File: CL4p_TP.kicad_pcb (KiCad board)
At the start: 2 copper layers, 75.4 x 74.9 mm, 23 parts, among them U1 MCP23017, X1 Badgelife_shitty_connector

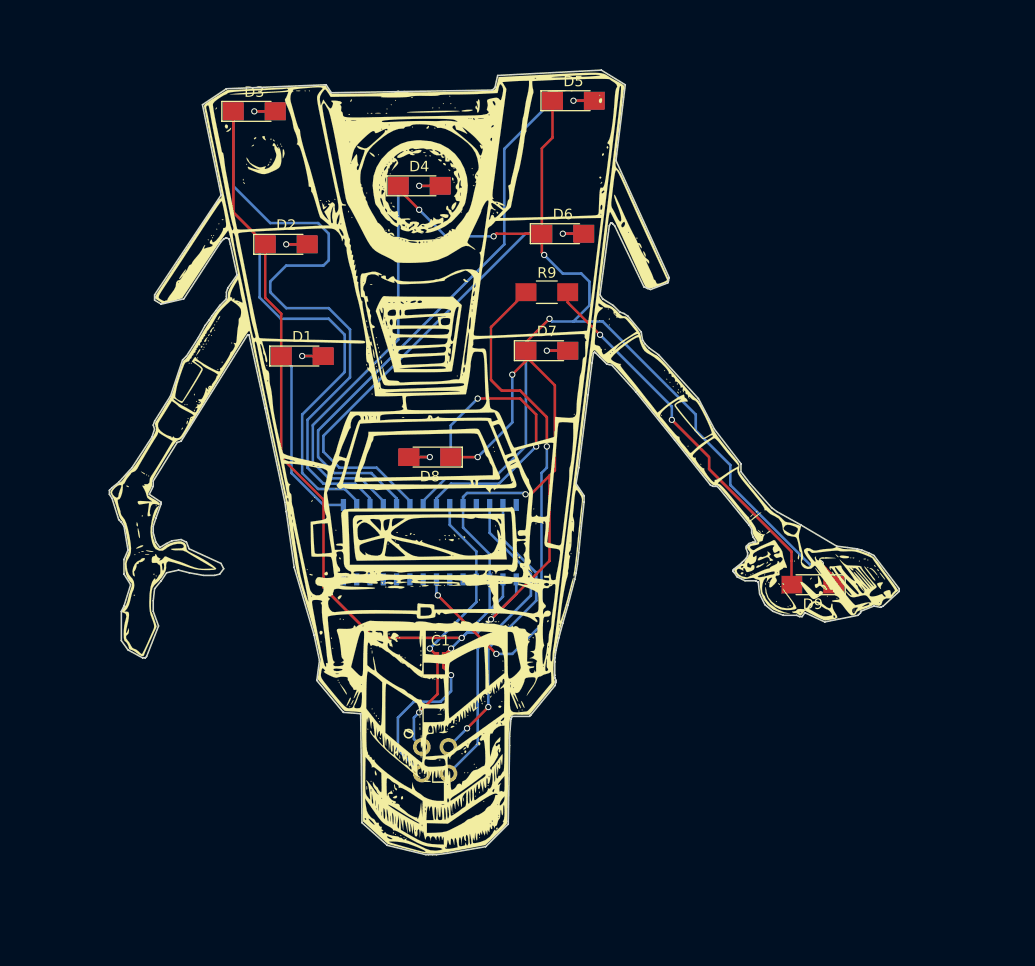
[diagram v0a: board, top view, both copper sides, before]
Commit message: Rev.2
Generated new gerbers for rev. 2.
Includes
-cleaned up paths utilizing ground plane and a larger plane between 3.3,Capacitor and MCP23017 Chip
-changed the mcp23017 chip from SOIC to SSOP
-modified single LED in middle of the board to recieve power directly off of the badge(just in case there is no I2C communication).
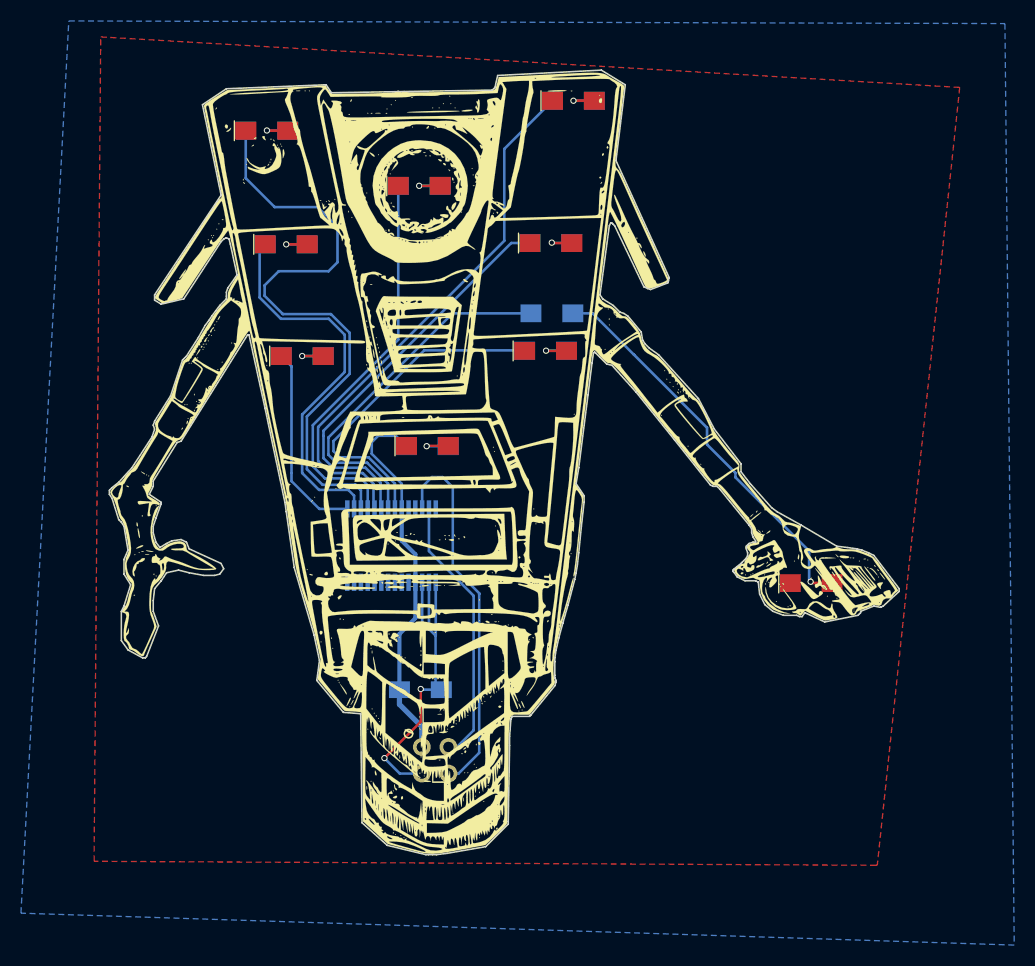
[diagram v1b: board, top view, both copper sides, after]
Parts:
- ? (x2): renamed from G***; value LOGO -> (none)
- C1: footprint Capacitors_SMD:C_0201_NoSilk -> lib:C_1206_HandSoldering_Min_Silk; moved to B.Cu
- D1, D2, D3, D4, D5, D6, D7, D8, D9: footprint LEDs:LED_1206_HandSoldering -> lib:LED_1206_HandSoldering_Min
- R1, R2, R3, R4, R5, R6, R7, R8: footprint Resistors_SMD:R_1206_HandSoldering -> lib:R_1206_HandSoldering_Min
- R9: footprint Resistors_SMD:R_1206_HandSoldering -> lib:R_1206_HandSoldering_Min; moved to B.Cu
- U1: footprint SMD_Packages:SOIC-28 -> lib:MCP23017-ESS_NoSilk
- moved D9 33.9 mm to (104.0, 98.6), turned to 0 degrees
- moved D7 33.6 mm to (129.4, 120.7)
- moved R9 5.58 mm to (104.0, 98.5)
- moved C1 3.92 mm to (92.1, 130.9)
- moved U1 3.67 mm to (89.3, 117.2), turned to 270 degrees
- moved R7 3.60 mm to (104.6, 95.0)
- moved D3 2.20 mm to (77.4, 77.5)
- moved R3 2.17 mm to (77.4, 77.5)
- moved R6 1.44 mm to (104.5, 88.3)
- moved D6 1.44 mm to (104.5, 88.3)
- moved D8 1.10 mm to (92.7, 107.6), turned to 0 degrees
- moved R8 1.07 mm to (92.7, 107.7)
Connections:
- R8 pad 1: Net-(R8-Pad1) -> Net-(D8-Pad2)
- R8 pad 2: Net-(D8-Pad2) -> +3V3
- U1 pad 21: Net-(R9-Pad1) -> Net-(U1-Pad21)
- U1 pad 8: Net-(R8-Pad1) -> Net-(R9-Pad1)
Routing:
- net GND: track 249.6 -> 35.2 mm, vias 12 -> 2
- net Net-(D7-Pad2): track 4.00 -> 38.3 mm
- net Net-(D9-Pad2): track 36.8 -> 3.91 mm, vias 2 -> 1
- net Net-(R8-Pad1): track 28.1 -> 0.00 mm, vias 2 -> 0
- net Net-(R9-Pad1): track 51.5 -> 32.3 mm, vias 3 -> 0
- net Net-(R7-Pad1): track 21.5 -> 35.2 mm
- net +3V3: track 27.7 -> 36.3 mm, vias 2 -> 0
- net scl: track 30.5 -> 36.0 mm
- net Net-(R6-Pad1): track 41.0 -> 38.7 mm
- net sda: track 27.9 -> 26.0 mm, vias 2 -> 0
- net Net-(R1-Pad1): track 17.8 -> 18.8 mm
- net Net-(R5-Pad1): track 53.1 -> 52.3 mm
- added copper zone on B.Cu, net GND
- added copper zone on F.Cu, net GND

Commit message: Tidying up
Uploading Copy used for final production
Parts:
- added G***: LOGO, Design:JACK2, B.Cu at (101.7, 106.8)
- U1: footprint lib:MCP23017-ESS_NoSilk -> lib:MCP23017-ESO_NoSilk
- moved U1 2.86 mm to (91.9, 118.3), turned to 0 degrees
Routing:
- net GND: track 35.2 -> 17.1 mm
- net Net-(R6-Pad1): track 38.7 -> 32.9 mm
- net Net-(R7-Pad1): track 35.2 -> 29.4 mm
- net Net-(R9-Pad1): track 32.3 -> 27.0 mm
- net Net-(R1-Pad1): track 18.8 -> 16.7 mm
- net sda: track 26.0 -> 27.4 mm
- net Net-(R2-Pad1): track 36.9 -> 35.9 mm
- net Net-(R3-Pad1): track 59.6 -> 59.0 mm
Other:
- board text added: "Thanks To:"
- board text added: "d4rkwyng AND!XOR"
- board text removed: "SpecialThanks to: d4rkwyng AND!XOR"
